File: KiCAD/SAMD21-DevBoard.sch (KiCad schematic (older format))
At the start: 23 parts, among them J1 .1\" Headers, J2 .1\" Headers, J3 Cortex_Debug, SW1 B3FS-4005P, U1 SAMD21G18A-AU, Y1 32.768KHz

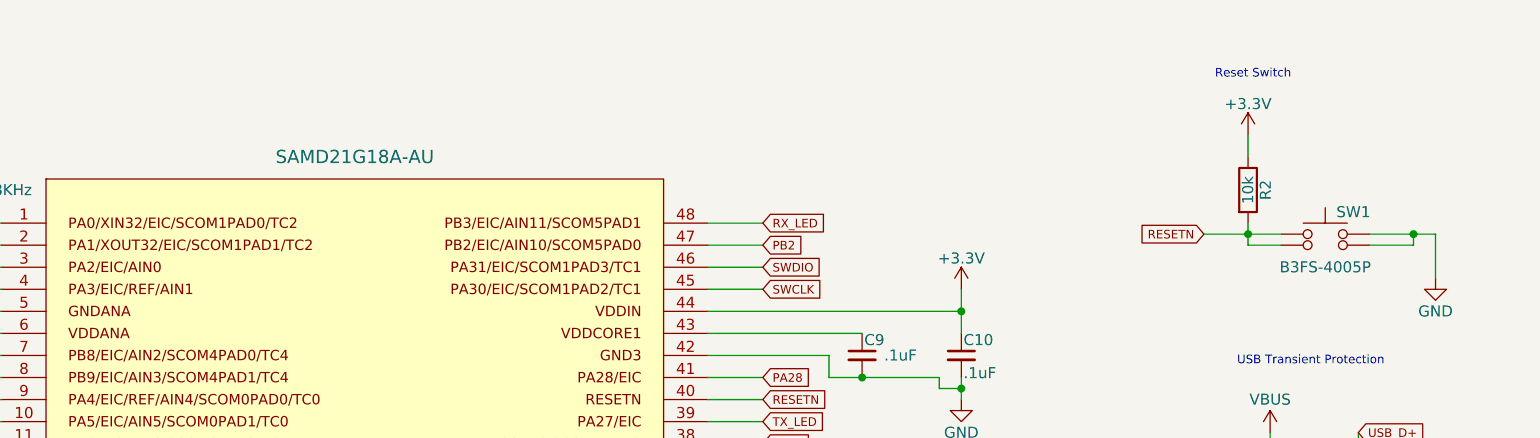
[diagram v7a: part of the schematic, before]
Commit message: Revising layout with different board outline
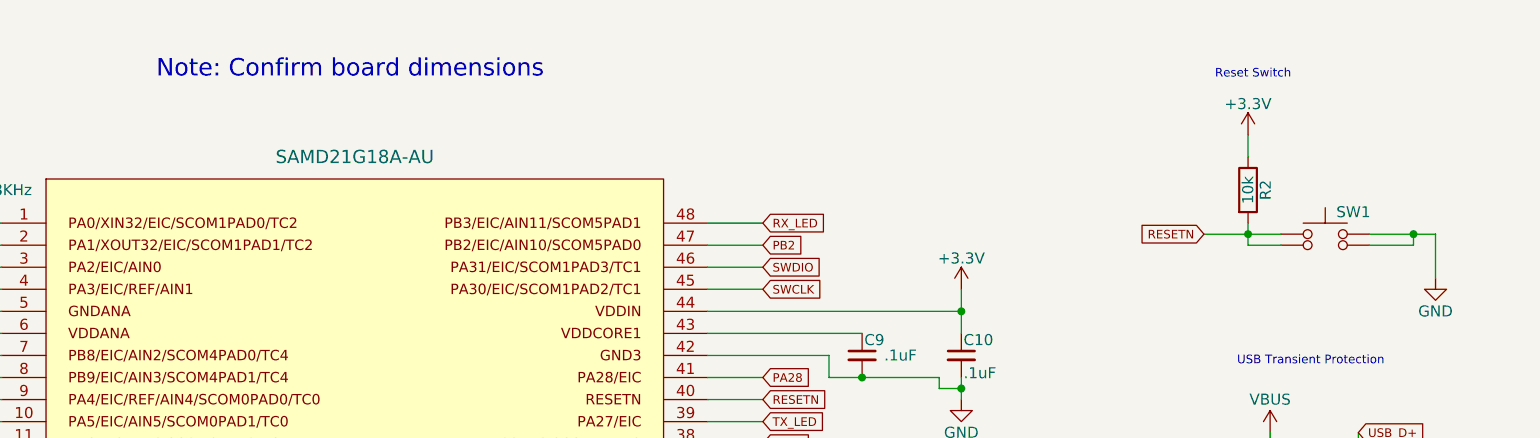
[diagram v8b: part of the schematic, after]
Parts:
- removed SW1: B3FS-4005P, B3FS-4:B3FS-4, symbol B3FS-4005P
- added SW1: FSMCTTR, FSMCTTR:FSMCTTR, symbol FSMCTTR
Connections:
- net GND: now also SW1.3, SW1.4
- net RESETN: now also SW1.1, SW1.2
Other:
- note added: "Note: Confirm board dimensions"
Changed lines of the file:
@@
 LIBS:B3FS-4005P
 LIBS:lm1117_edited
+LIBS:fsmcttr
 LIBS:SAMD21-DevBoard-cache
 EELAYER 25 0
@@
 	4800 5550 4150 5550
 Connection ~ 4150 5550
-$Comp
-L B3FS-4005P SW1
-U 1 1 5C02E356
-P 8900 1850
-F 0 "SW1" H 8950 1950 50  0000 L CNN
-F 1 "B3FS-4005P" H 8900 1700 50  0000 C CNN
-F 2 "B3FS-4:B3FS-4" H 8900 2050 50  0001 C CNN
-F 3 "" H 8900 2050 50  0001 C CNN
-	1    8900 1850
-	1    0    0    -1
-$EndComp
 Connection ~ 8550 1850
 Wire Wire Line
@@
 	1    0    0    -1
 $EndComp
+Text Notes 3600 1150 0    79   ~ 0
+Note: Confirm board dimensions
+$Comp
+L FSMCTTR SW1
+U 1 1 5C1D3C4B
+P 8900 1850
+F 0 "SW1" H 8950 1950 50  0000 L CNN
+F 1 "FSMCTTR" H 8900 1700 50  0001 C CNN
+F 2 "FSMCTTR:FSMCTTR" H 8900 2050 50  0001 C CNN
+F 3 "" H 8900 2050 50  0001 C CNN
+	1    8900 1850
+	1    0    0    -1
+$EndComp
